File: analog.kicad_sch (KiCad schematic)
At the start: 27 parts, among them U2 AD9833xRM, U4 LM4881M

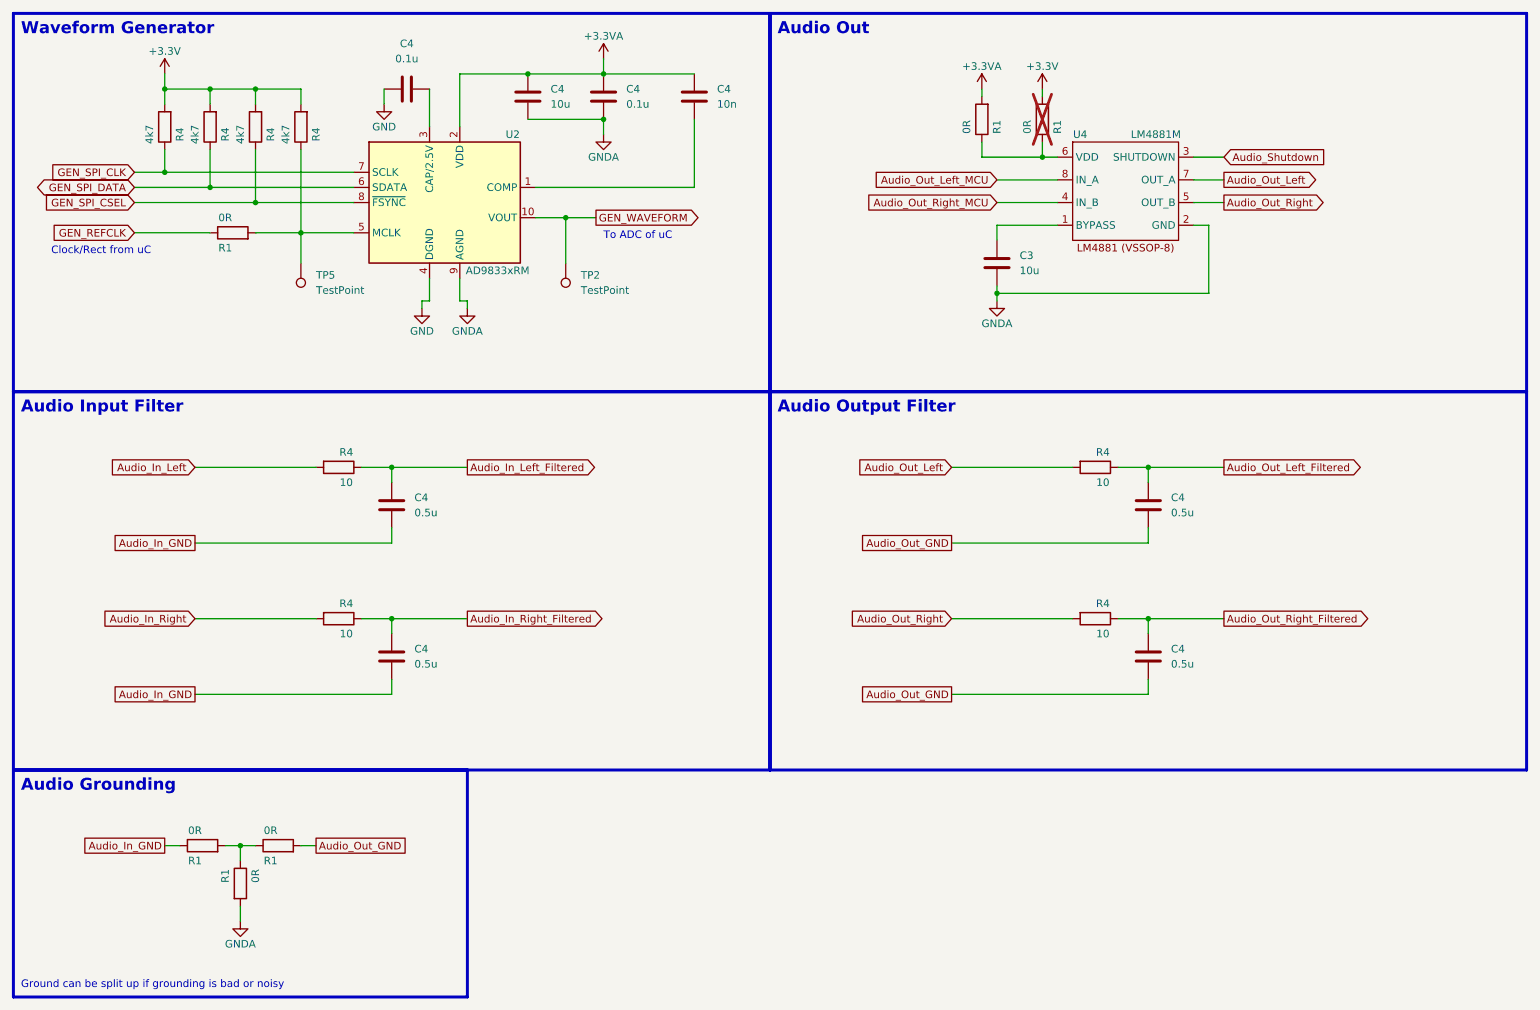
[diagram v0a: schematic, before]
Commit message: Added ESD, updated Footprints, BOM, etc.
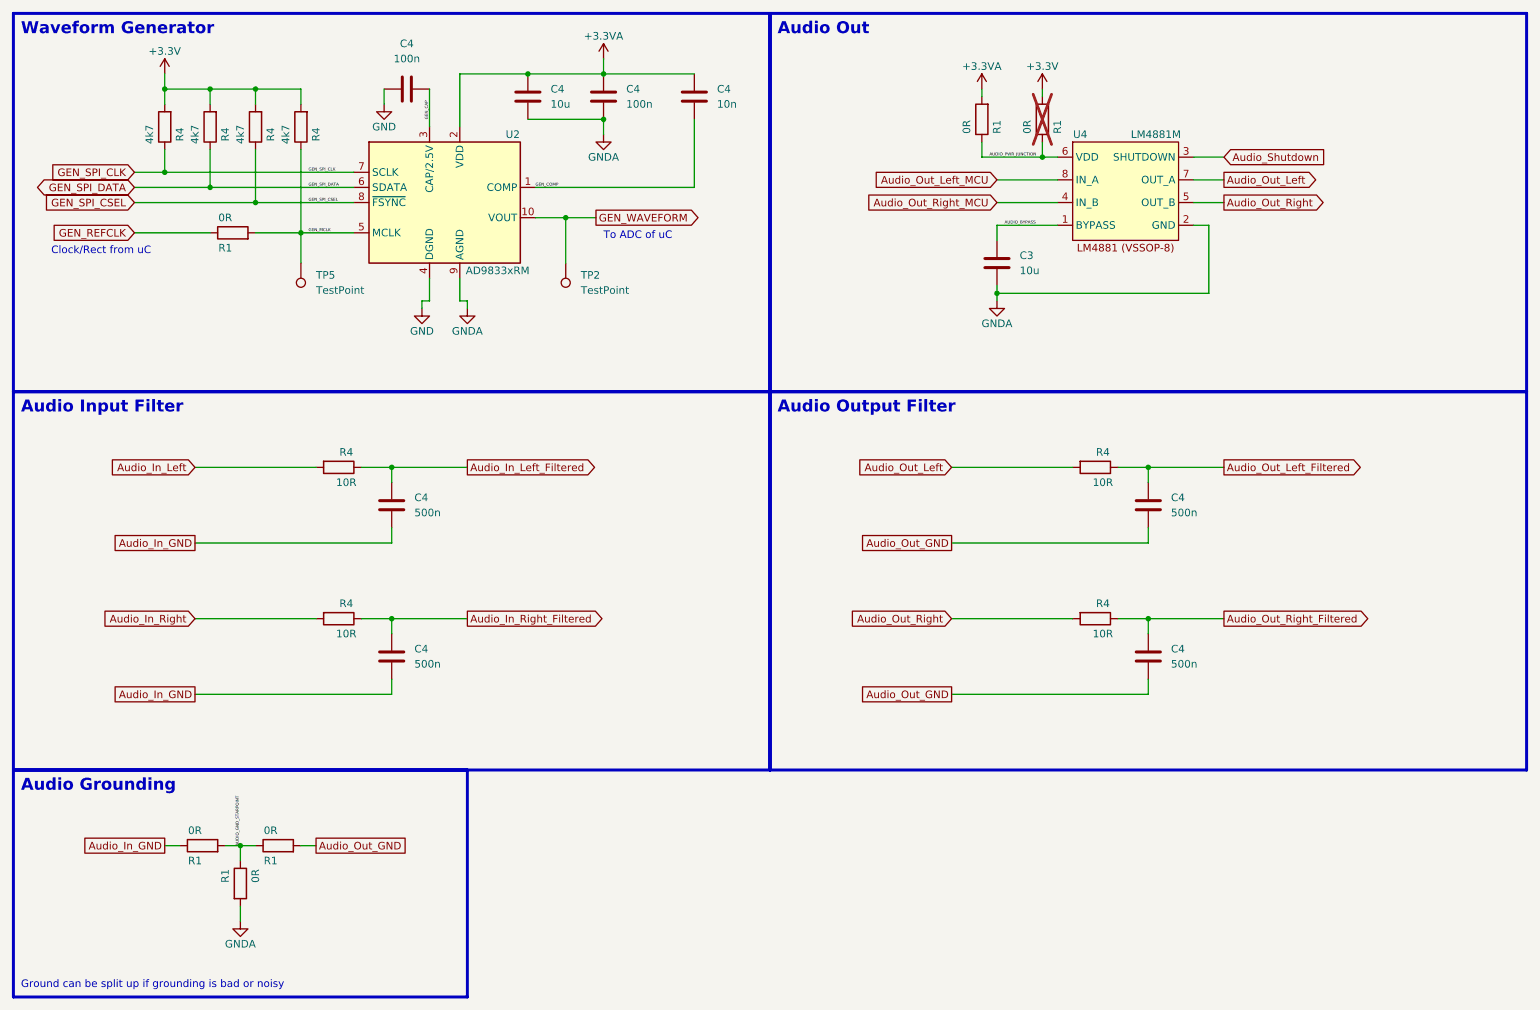
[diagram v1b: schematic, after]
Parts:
- C4: value 0.5u -> 500n
- C4: value 0.1u -> 100n
- R4: value 10 -> 10R
- TP2, TP5: now left out of the parts list
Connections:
- net AUDIO_GND_STARPOINT: now reaches R1.1, R1.1, R1.2
- net AUDIO_BYPASS: now reaches C3.1, U4.1 (BYPASS)
- net AUDIO_PWR_JUNCTION: now reaches R1.1, R1.1, U4.6 (VDD)
- net GEN_COMP: now reaches C4.2, U2.1 (COMP)
- net GEN_CAP: now reaches C4.2, U2.3 (CAP/2.5V)
- net GEN_MCLK: now reaches R1.2, R4.1, TP5.1, U2.5 (MCLK)

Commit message: Schematic is done for now, starting layout
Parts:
- U2: Distributor Link (none) -> https://www.mouser.de/ProductDetail/Analog-Devices/AD9833BR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; Manufacturer (none) -> Analog Devices; Manufacturer Number (none) -> AD9833BRMZ
- U4: Distributor Link (none) -> https://www.mouser.de/ProductDetail/Texas-Instruments/LM488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; Manufacturer (none) -> Texas Instruments; Manufacturer Number (none) -> LM4881MM/NOPB
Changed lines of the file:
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@@
+      (effects (font (size 1.27 1.27)) hide)
+    )
+    (property "Distributor Link" "" (at 118.11 67.31 0)
+      (effects (font (size 1.27 1.27)) hide)
+    )
+    (property "Manufacturer" "" (at 118.11 67.31 0)
       (effects (font (size 1.27 1.27)) hide)
     )
@@
       (effects (font (size 1.27 1.27)) hide)
     )
+    (property "Distributor Link" "" (at 80.01 127 0)
+      (effects (font (size 1.27 1.27)) hide)
+    )
+    (property "Manufacturer" "" (at 80.01 127 0)
+      (effects (font (size 1.27 1.27)) hide)
+    )
     (pin "1")
     (pin "2")
@@
       (effects (font (size 1.27 1.27)) hide)
     )
+    (property "Distributor Link" "" (at 63.5 171.45 0)
+      (effects (font (size 1.27 1.27)) hide)
+    )
+    (property "Manufacturer" "" (at 63.5 171.45 0)
+      (effects (font (size 1.27 1.27)) hide)
+    )
     (pin "1")
     (pin "2")
@@
     )
     (property "Datasheet" "~" (at 207.01 127 0)
+      (effects (font (size 1.27 1.27)) hide)
+    )
+    (property "Distributor Link" "" (at 207.01 127 0)
+      (effects (font (size 1.27 1.27)) hide)
+    )
+    (property "Manufacturer" "" (at 207.01 127 0)
       (effects (font (size 1.27 1.27)) hide)
     )
@@
       (effects (font (size 1.27 1.27)) hide)
     )
+    (property "Distributor Link" "" (at 215.9 107.95 0)
+      (effects (font (size 1.27 1.27)) hide)
+    )
+    (property "Manufacturer" "" (at 215.9 107.95 0)
+      (effects (font (size 1.27 1.27)) hide)
+    )
     (pin "1")
     (pin "2")
@@
       (effects (font (size 1.27 1.27)) hide)
     )
+    (property "Distributor Link" "" (at 215.9 133.35 0)
+      (effects (font (size 1.27 1.27)) hide)
+    )
+    (property "Manufacturer" "" (at 215.9 133.35 0)
+      (effects (font (size 1.27 1.27)) hide)
+    )
     (pin "1")
     (pin "2")
@@
       (effects (font (size 1.27 1.27)) hide)
     )
+    (property "Manufacturer Number" "LM4881MM/NOPB" (at 231.14 64.77 0)
+      (effects (font (size 1.27 1.27)) hide)
+    )
+    (property "Mechanical Outline Drawing" "https://www.ti.com/lit/ml/mpds028d/mpds028d.pdf?ts=1704435799998" (at 210.82 69.85 0)
+      (effects (font (size 1.27 1.27)) hide)
+    )
+    (property "Distributor Link" "https://www.mouser.de/ProductDetail/Texas-Instruments/LM4881MM-NOPB?qs=QbsRYf82W3Fa5MwtH%252B770A%3D%3D" (at 207.01 54.61 0)
+      (effects (font (size 1.27 1.27)) hide)
+    )
+    (property "Manufacturer" "Texas Instruments" (at 207.01 54.61 0)
+      (effects (font (size 1.27 1.27)) hide)
+    )
     (property "MFN" "LM4881MM/NOPB" (at 231.14 64.77 0)
-      (effects (font (size 1.27 1.27)) hide)
-    )
-    (property "Mechanical Outline Drawing" "https://www.ti.com/lit/ml/mpds028d/mpds028d.pdf?ts=1704435799998" (at 210.82 69.85 0)
       (effects (font (size 1.27 1.27)) hide)
     )
@@
       (effects (font (size 1.27 1.27)) hide)
     )
+    (property "Distributor Link" "" (at 111.76 39.37 0)
+      (effects (font (size 1.27 1.27)) hide)
+    )
+    (property "Manufacturer" "" (at 111.76 39.37 0)
+      (effects (font (size 1.27 1.27)) hide)
+    )
     (pin "1")
     (pin "2")
@@
     )
     (property "Datasheet" "https://www.analog.com/media/en/technical-documentation/data-sheets/ad9833.pdf" (at 96.52 49.53 0)
+      (effects (font (size 1.27 1.27)) hide)
+    )
+    (property "Distributor Link" "https://www.mouser.de/ProductDetail/Analog-Devices/AD9833BRMZ?qs=BpaRKvA4VqFt3Bdw9RBKCQ%3D%3D" (at 97.79 57.15 0)
+      (effects (font (size 1.27 1.27)) hide)
+    )
+    (property "Manufacturer" "Analog Devices" (at 97.79 57.15 0)
+      (effects (font (size 1.27 1.27)) hide)
+    )
+    (property "Manufacturer Number" "AD9833BRMZ" (at 97.79 57.15 0)
       (effects (font (size 1.27 1.27)) hide)
     )
@@
       (effects (font (size 1.27 1.27)) hide)
     )
+    (property "Distributor Link" "" (at 124.46 39.37 0)
+      (effects (font (size 1.27 1.27)) hide)
+    )
+    (property "Manufacturer" "" (at 124.46 39.37 0)
+      (effects (font (size 1.27 1.27)) hide)
+    )
     (pin "1")
     (pin "2")
@@
       (effects (font (size 1.27 1.27)) hide)
     )
+    (property "Distributor Link" "" (at 207.01 101.6 0)
+      (effects (font (size 1.27 1.27)) hide)
+    )
+    (property "Manufacturer" "" (at 207.01 101.6 0)
+      (effects (font (size 1.27 1.27)) hide)
+    )
     (pin "1")
     (pin "2")
@@
     )
     (property "Datasheet" "~" (at 50.8 44.45 0)
+      (effects (font (size 1.27 1.27)) hide)
+    )
+    (property "Distributor Link" "" (at 50.8 44.45 0)
+      (effects (font (size 1.27 1.27)) hide)
+    )
+    (property "Manufacturer" "" (at 50.8 44.45 0)
       (effects (font (size 1.27 1.27)) hide)
     )
@@
       (effects (font (size 1.27 1.27)) hide)
     )
+    (property "Distributor Link" "" (at 190.5 67.31 0)
+      (effects (font (size 1.27 1.27)) hide)
+    )
+    (property "Manufacturer" "" (at 190.5 67.31 0)
+      (effects (font (size 1.27 1.27)) hide)
+    )
     (pin "1")
     (pin "2")
@@
     )
     (property "Datasheet" "~" (at 58.42 44.45 0)
+      (effects (font (size 1.27 1.27)) hide)
+    )
+    (property "Distributor Link" "" (at 58.42 44.45 0)
+      (effects (font (size 1.27 1.27)) hide)
+    )
+    (property "Manufacturer" "" (at 58.42 44.45 0)
       (effects (font (size 1.27 1.27)) hide)
     )
@@
       (effects (font (size 1.27 1.27)) hide)
     )
+    (property "Distributor Link" "" (at 198.12 43.18 0)
+      (effects (font (size 1.27 1.27)) hide)
+    )
+    (property "Manufacturer" "" (at 198.12 43.18 0)
+      (effects (font (size 1.27 1.27)) hide)
+    )
     (pin "1")
     (pin "2")
@@
       (effects (font (size 1.27 1.27)) hide)
     )
+    (property "Distributor Link" "" (at 88.9 107.95 0)
+      (effects (font (size 1.27 1.27)) hide)
+    )
+    (property "Manufacturer" "" (at 88.9 107.95 0)
+      (effects (font (size 1.27 1.27)) hide)
+    )
     (pin "1")
     (pin "2")
@@
     )
     (property "Datasheet" "~" (at 62.23 62.23 0)
+      (effects (font (size 1.27 1.27)) hide)
+    )
+    (property "Distributor Link" "" (at 62.23 62.23 0)
+      (effects (font (size 1.27 1.27)) hide)
+    )
+    (property "Manufacturer" "" (at 62.23 62.23 0)
       (effects (font (size 1.27 1.27)) hide)
     )
@@
       (effects (font (size 1.27 1.27)) hide)
     )
+    (property "Distributor Link" "" (at 88.9 133.35 0)
+      (effects (font (size 1.27 1.27)) hide)
+    )
+    (property "Manufacturer" "" (at 88.9 133.35 0)
+      (effects (font (size 1.27 1.27)) hide)
+    )
     (pin "1")
     (pin "2")
@@
     )
     (property "Datasheet" "~" (at 69.85 165.1 0)
+      (effects (font (size 1.27 1.27)) hide)
+    )
+    (property "Distributor Link" "" (at 69.85 165.1 0)
+      (effects (font (size 1.27 1.27)) hide)
+    )
+    (property "Manufacturer" "" (at 69.85 165.1 0)
       (effects (font (size 1.27 1.27)) hide)
     )
@@
       (effects (font (size 1.27 1.27)) hide)
     )
+    (property "Distributor Link" "" (at 139.7 39.37 0)
+      (effects (font (size 1.27 1.27)) hide)
+    )
+    (property "Manufacturer" "" (at 139.7 39.37 0)
+      (effects (font (size 1.27 1.27)) hide)
+    )
     (pin "1")
     (pin "2")
@@
       (effects (font (size 1.27 1.27)) hide)
     )
+    (property "Distributor Link" "" (at 187.96 43.18 0)
+      (effects (font (size 1.27 1.27)) hide)
+    )
+    (property "Manufacturer" "" (at 187.96 43.18 0)
+      (effects (font (size 1.27 1.27)) hide)
+    )
     (pin "1")
     (pin "2")
@@
       (effects (font (size 1.27 1.27)) hide)
     )
+    (property "Distributor Link" "" (at 80.01 101.6 0)
+      (effects (font (size 1.27 1.27)) hide)
+    )
+    (property "Manufacturer" "" (at 80.01 101.6 0)
+      (effects (font (size 1.27 1.27)) hide)
+    )
     (pin "1")
     (pin "2")
@@
     )
     (property "Datasheet" "~" (at 73.66 44.45 0)
+      (effects (font (size 1.27 1.27)) hide)
+    )
+    (property "Distributor Link" "" (at 73.66 44.45 0)
+      (effects (font (size 1.27 1.27)) hide)
+    )
+    (property "Manufacturer" "" (at 73.66 44.45 0)
       (effects (font (size 1.27 1.27)) hide)
     )
@@
       (effects (font (size 1.27 1.27)) hide)
     )
+    (property "Distributor Link" "" (at 91.44 38.1 0)
+      (effects (font (size 1.27 1.27)) hide)
+    )
+    (property "Manufacturer" "" (at 91.44 38.1 0)
+      (effects (font (size 1.27 1.27)) hide)
+    )
     (pin "1")
     (pin "2")
@@
     )
     (property "Datasheet" "~" (at 66.04 44.45 0)
+      (effects (font (size 1.27 1.27)) hide)
+    )
+    (property "Distributor Link" "" (at 66.04 44.45 0)
+      (effects (font (size 1.27 1.27)) hide)
+    )
+    (property "Manufacturer" "" (at 66.04 44.45 0)
       (effects (font (size 1.27 1.27)) hide)
     )
@@
       (effects (font (size 1.27 1.27)) hide)
     )
+    (property "Distributor Link" "" (at 73.66 67.31 0)
+      (effects (font (size 1.27 1.27)) hide)
+    )
+    (property "Manufacturer" "" (at 73.66 67.31 0)
+      (effects (font (size 1.27 1.27)) hide)
+    )
     (pin "1")
     (instances
@@
       (effects (font (size 1.27 1.27)) hide)
     )
+    (property "Distributor Link" "" (at 57.15 165.1 0)
+      (effects (font (size 1.27 1.27)) hide)
+    )
+    (property "Manufacturer" "" (at 57.15 165.1 0)
+      (effects (font (size 1.27 1.27)) hide)
+    )

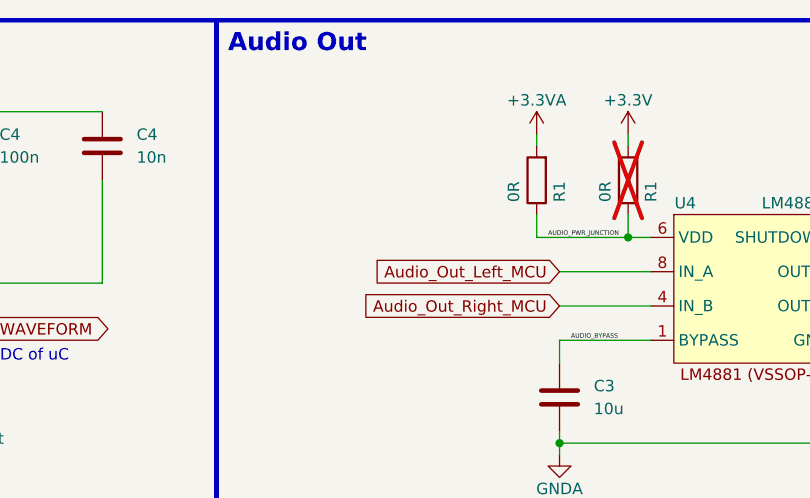
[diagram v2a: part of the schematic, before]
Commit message: Layout done, footprints mostly assigned, 3D models assigned if not annoying to get. Few TODOs left and they are marked on the PCB.
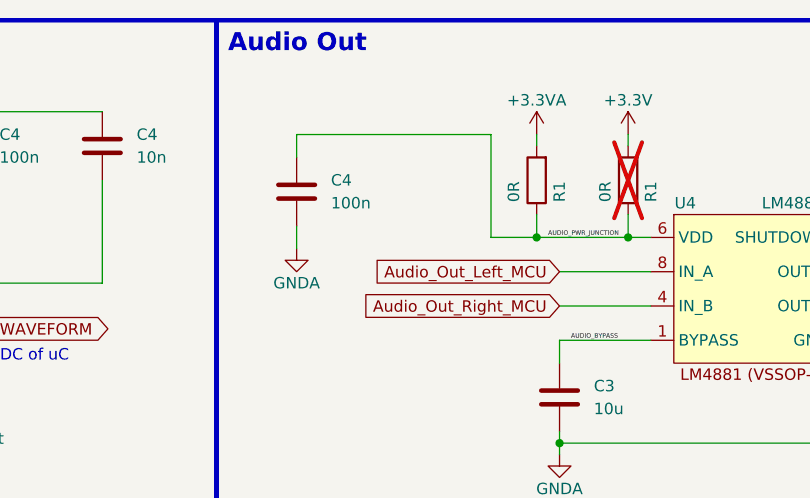
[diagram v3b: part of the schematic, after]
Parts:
- added C4: 100n, Capacitor_SMD:C_0603_1608Metric, symbol Device:C
- R1: footprint Resistor_SMD:R_0805_2012Metric -> Resistor_SMD:R_0402_1005Metric
- U4: MFN LM4881MM/NOPB -> (none)
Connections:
- net AUDIO_PWR_JUNCTION: now also C4.1
- net GNDA: now also C4.2
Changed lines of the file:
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@@
   (junction (at 215.9 127) (diameter 0) (color 0 0 0 0)
   )
+  (junction (at 187.96 49.53) (diameter 0) (color 0 0 0 0)
+  )
   (junction (at 190.5 72.39) (diameter 0) (color 0 0 0 0)
   )
@@
     (stroke (width 0) (type default))
   )
+  (wire (pts (xy 187.96 49.53) (xy 182.88 49.53))
+    (stroke (width 0) (type default))
+  )
+  (wire (pts (xy 161.29 50.8) (xy 161.29 48.26))
+    (stroke (width 0) (type default))
+  )
   (wire (pts (xy 55.88 101.6) (xy 76.2 101.6))
     (stroke (width 0) (type default))
@@
     (stroke (width 0) (type default))
   )
+  (wire (pts (xy 161.29 38.1) (xy 161.29 40.64))
+    (stroke (width 0) (type default))
+  )
   (wire (pts (xy 50.8 165.1) (xy 53.34 165.1))
     (stroke (width 0) (type default))
@@
     (stroke (width 0) (type default))
   )
+  (wire (pts (xy 182.88 38.1) (xy 161.29 38.1))
+    (stroke (width 0) (type default))
+  )
   (wire (pts (xy 83.82 127) (xy 88.9 127))
     (stroke (width 0) (type default))
@@
   )
   (wire (pts (xy 50.8 48.26) (xy 50.8 52.07))
+    (stroke (width 0) (type default))
+  )
+  (wire (pts (xy 182.88 49.53) (xy 182.88 38.1))
     (stroke (width 0) (type default))
   )
@@
       (effects (font (size 1.27 1.27)) hide)
     )
-    (property "MFN" "LM4881MM/NOPB" (at 231.14 64.77 0)
+    (property "MFN" "" (at 231.14 64.77 0)
       (effects (font (size 1.27 1.27)) hide)
     )
@@
       (effects (font (size 1.27 1.27)))
     )
-    (property "Footprint" "Resistor_SMD:R_0805_2012Metric" (at 62.23 64.008 90)
+    (property "Footprint" "Resistor_SMD:R_0402_1005Metric" (at 62.23 64.008 90)
       (effects (font (size 1.27 1.27)) hide)
     )
@@
     )
   )
+  (symbol (lib_id "power:GNDA") (at 161.29 50.8 0) (unit 1)
+    (in_bom yes) (on_board yes) (dnp no)
+    (property "Reference" "#PWR07" (at 161.29 57.15 0)
+      (effects (font (size 1.27 1.27)) hide)
+    )
+    (property "Value" "GNDA" (at 161.29 54.61 0)
+      (effects (font (size 1.27 1.27)))
+    )
+    (property "Footprint" "" (at 161.29 50.8 0)
+      (effects (font (size 1.27 1.27)) hide)
+    )
+    (property "Datasheet" "" (at 161.29 50.8 0)
+      (effects (font (size 1.27 1.27)) hide)
+    )
+    (pin "1")
+    (instances
+      (project "schneidbrett"
+        (path "/c05974a1-d9e7-44bd-b1f3-81c4ede4353c/86ba3294-cf4a-47ab-b34c-9be2b0ce2123"
+          (reference "#PWR07") (unit 1)
+        )
+        (path "/c05974a1-d9e7-44bd-b1f3-81c4ede4353c/b0bd55ef-d145-4fa7-a843-05d41e852979"
+          (reference "#PWR015") (unit 1)
+        )
+        (path "/c05974a1-d9e7-44bd-b1f3-81c4ede4353c/88b5b5f9-c416-4523-9e04-323b913d1bb0"
+          (reference "#PWR025") (unit 1)
+        )
+      )
+    )
+  )
   (symbol (lib_id "power:GNDA") (at 63.5 177.8 0) (unit 1)
     (in_bom yes) (on_board yes) (dnp no)
@@
         )
       )
+    )
+  )
+  (symbol (lib_id "Device:C") (at 161.29 44.45 0) (unit 1)
+    (in_bom yes) (on_board yes) (dnp no) (fields_autoplaced)
+    (property "Reference" "C4" (at 165.1 43.18 0)
+      (effects (font (size 1.27 1.27)) (justify left))
+    )
+    (property "Value" "100n" (at 165.1 45.72 0)
+      (effects (font (size 1.27 1.27)) (justify left))
+    )
+    (property "Footprint" "Capacitor_SMD:C_0603_1608Metric" (at 162.2552 48.26 0)
+      (effects (font (size 1.27 1.27)) hide)
+    )
+    (property "Datasheet" "~" (at 161.29 44.45 0)
+      (effects (font (size 1.27 1.27)) hide)
+    )
+    (property "Distributor Link" "" (at 161.29 44.45 0)
+      (effects (font (size 1.27 1.27)) hide)
+    )
+    (property "Manufacturer" "" (at 161.29 44.45 0)
+      (effects (font (size 1.27 1.27)) hide)
+    )
+    (pin "1")
+    (pin "2")
+    (instances
+      (project "schneidbrett"
+        (path "/c05974a1-d9e7-44bd-b1f3-81c4ede4353c/86ba3294-cf4a-47ab-b34c-9be2b0ce2123"
+          (reference "C4") (unit 1)
+        )
+        (path "/c05974a1-d9e7-44bd-b1f3-81c4ede4353c/88b5b5f9-c416-4523-9e04-323b913d1bb0"
+          (reference "C6") (unit 1)
+        )
+      )
